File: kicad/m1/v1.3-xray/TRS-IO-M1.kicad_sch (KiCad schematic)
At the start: 29 parts, among them J1 Conn_02x20_Odd_Even, J2 Conn_02x20_Odd_Even, J3 Conn_01x02_Male, J4 Conn_01x02_Male, J5 Conn_01x02_Male, Q1 2N7000, Q2 2N7000, SW1 SW_Push, U1 SN74LVCH8T245, U2 74LVC245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

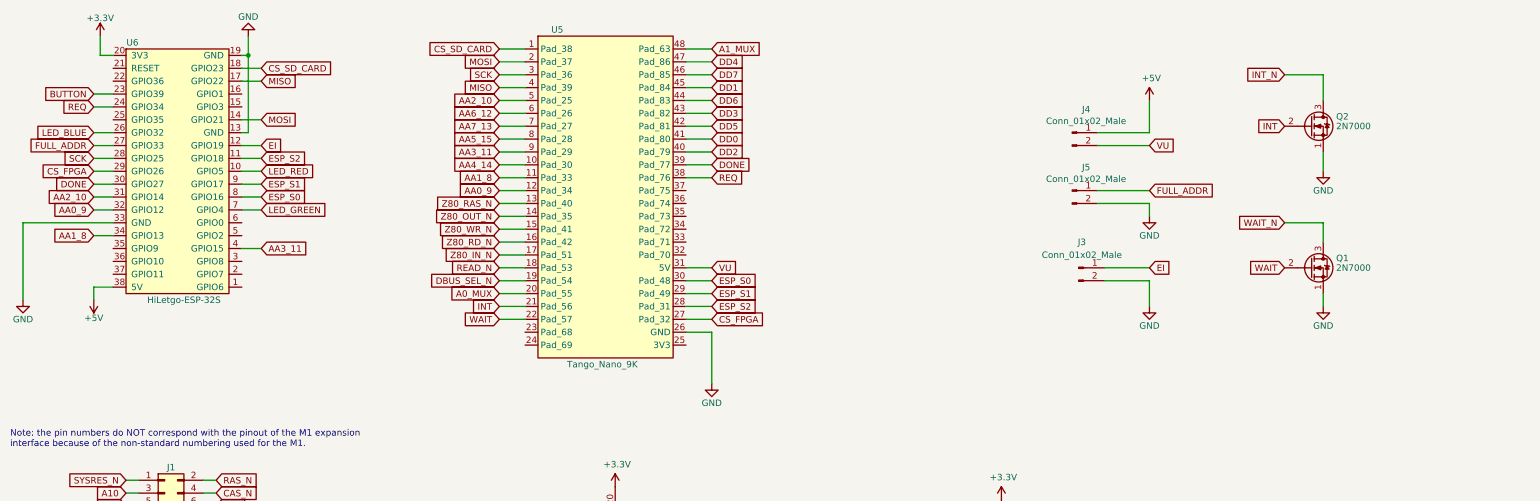
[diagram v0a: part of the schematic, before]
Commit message: PCB updates for TRS-IO-M1 1.3
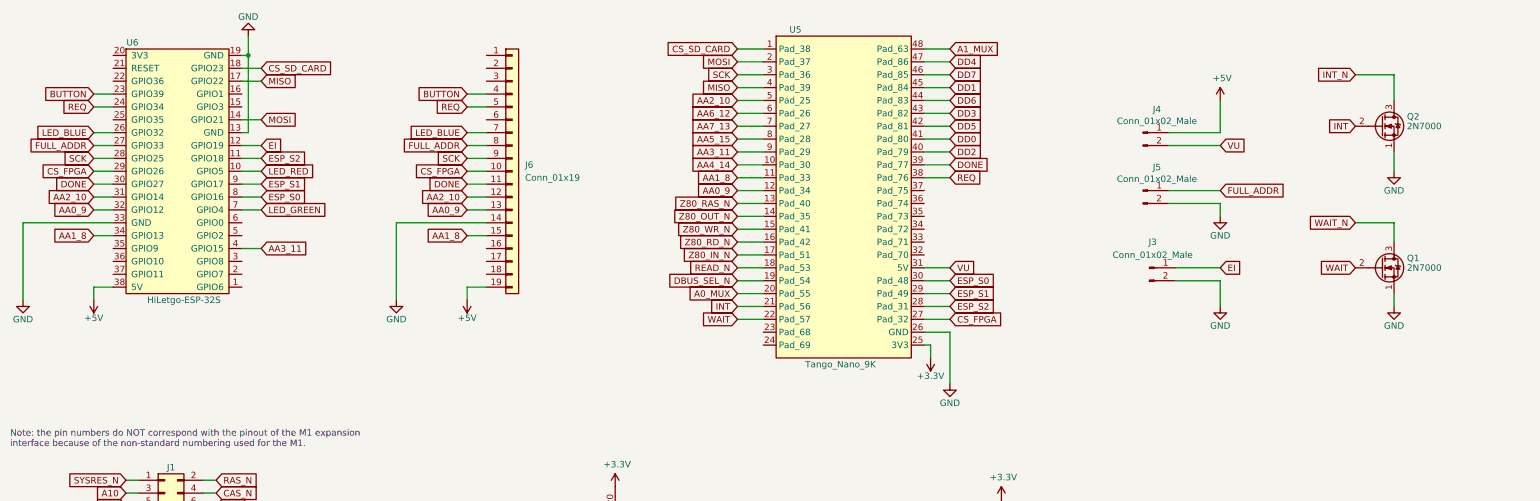
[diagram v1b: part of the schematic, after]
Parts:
- added J6: Conn_01x19, Connector_PinHeader_2.54mm:PinHeader_1x19_P2.54mm_Vertical, symbol Connector_Generic:Conn_01x19
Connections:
- net +3V3: now also U5.25 (3V3); no longer U6.20 (3V3)
- net +5V: now also J6.19 (Pin_19)
- net AA0_9: now also J6.13 (Pin_13)
- net AA1_8: now also J6.15 (Pin_15)
- net AA2_10: now also J6.12 (Pin_12)
- net BUTTON: now also J6.4 (Pin_4)
- net CS_FPGA: now also J6.10 (Pin_10)
- net DONE: now also J6.11 (Pin_11)
- net FULL_ADDR: now also J6.8 (Pin_8)
- net GND: now also J6.14 (Pin_14)
- net LED_BLUE: now also J6.7 (Pin_7)
- net REQ: now also J6.5 (Pin_5)
- net SCK: now also J6.9 (Pin_9)
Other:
- moved on the sheet: J3, J4, J5, Q1, Q2, U5
